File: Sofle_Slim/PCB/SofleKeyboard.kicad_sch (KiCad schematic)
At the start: 103 parts, among them J2 4PIN, J3 OLED, P1 i2c_pin, P2 i2c_pin, P3 USB_C_Plug_USB2.0, SW1 SW_PUSH_LED, SW10 SW_PUSH_LED, SW11 SW_PUSH_LED, SW12 SW_PUSH_LED, SW13 SW_PUSH_LED, SW14 SW_PUSH_LED, SW15 SW_PUSH_LED, SW16 SW_PUSH_LED, SW17 SW_PUSH_LED, SW18 SW_PUSH_LED, SW19 SW_PUSH_LED, SW2 SW_PUSH_LED, SW20 SW_PUSH_LED, SW21 SW_PUSH_LED, SW22 SW_PUSH_LED, SW23 SW_PUSH_LED, SW24 SW_PUSH_LED, SW25 Rotary_Encoder_Switch, SW26 SW_PUSH_LED, SW27 SW_PUSH_LED, SW28 SW_PUSH_LED, SW29 SW_PUSH_LED, SW3 SW_PUSH_LED, SW30 SW_PUSH_LED, SW4 SW_PUSH_LED, SW5 SW_PUSH_LED, SW6 SW_PUSH_LED, SW7 SW_PUSH_LED, SW8 SW_PUSH_LED, SW9 SW_PUSH_LED, U1 ProMicro, U2 ATmega32U4-A, Y1 16MHz

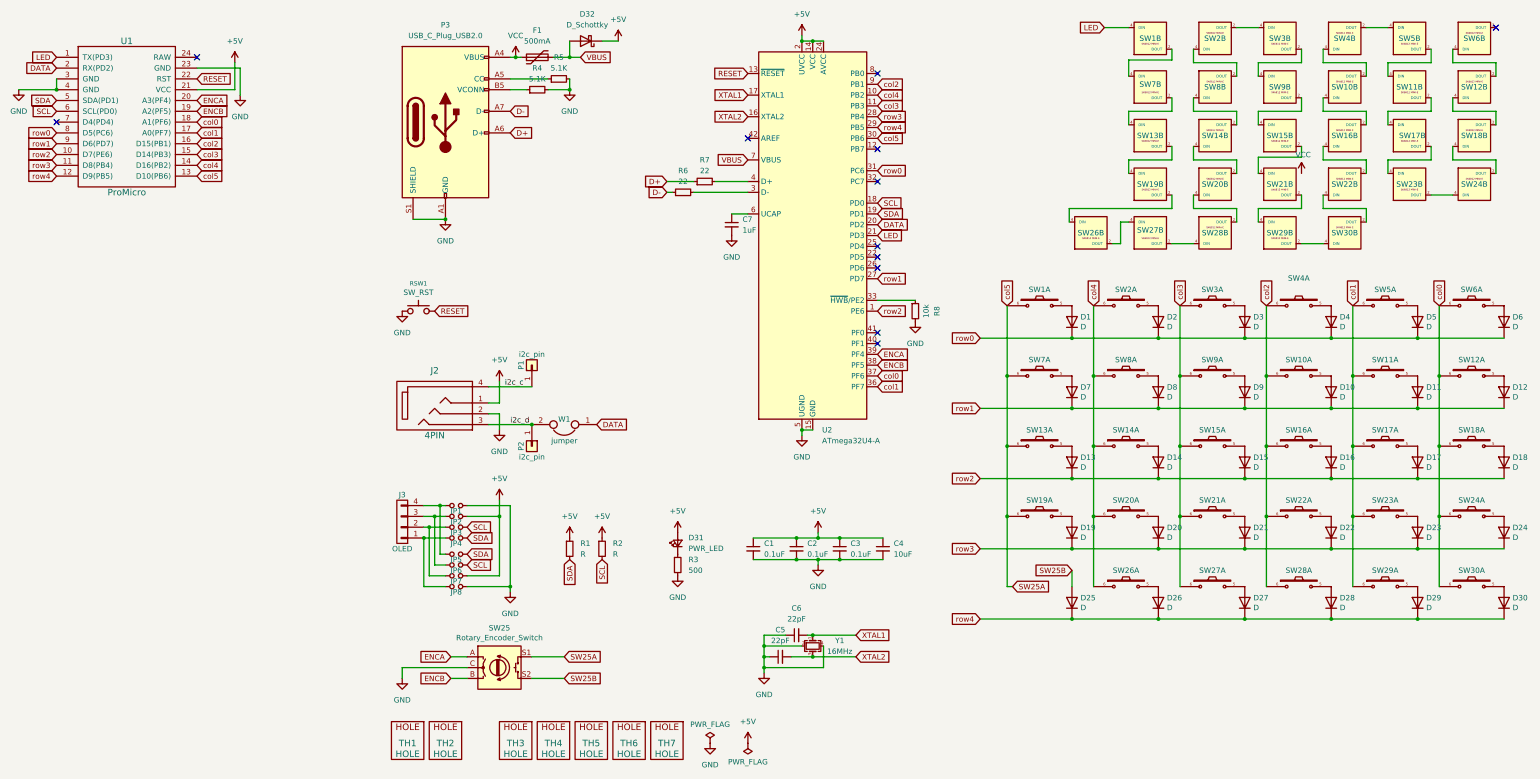
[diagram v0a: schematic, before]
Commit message: changed usb-c plug for usb receptacle
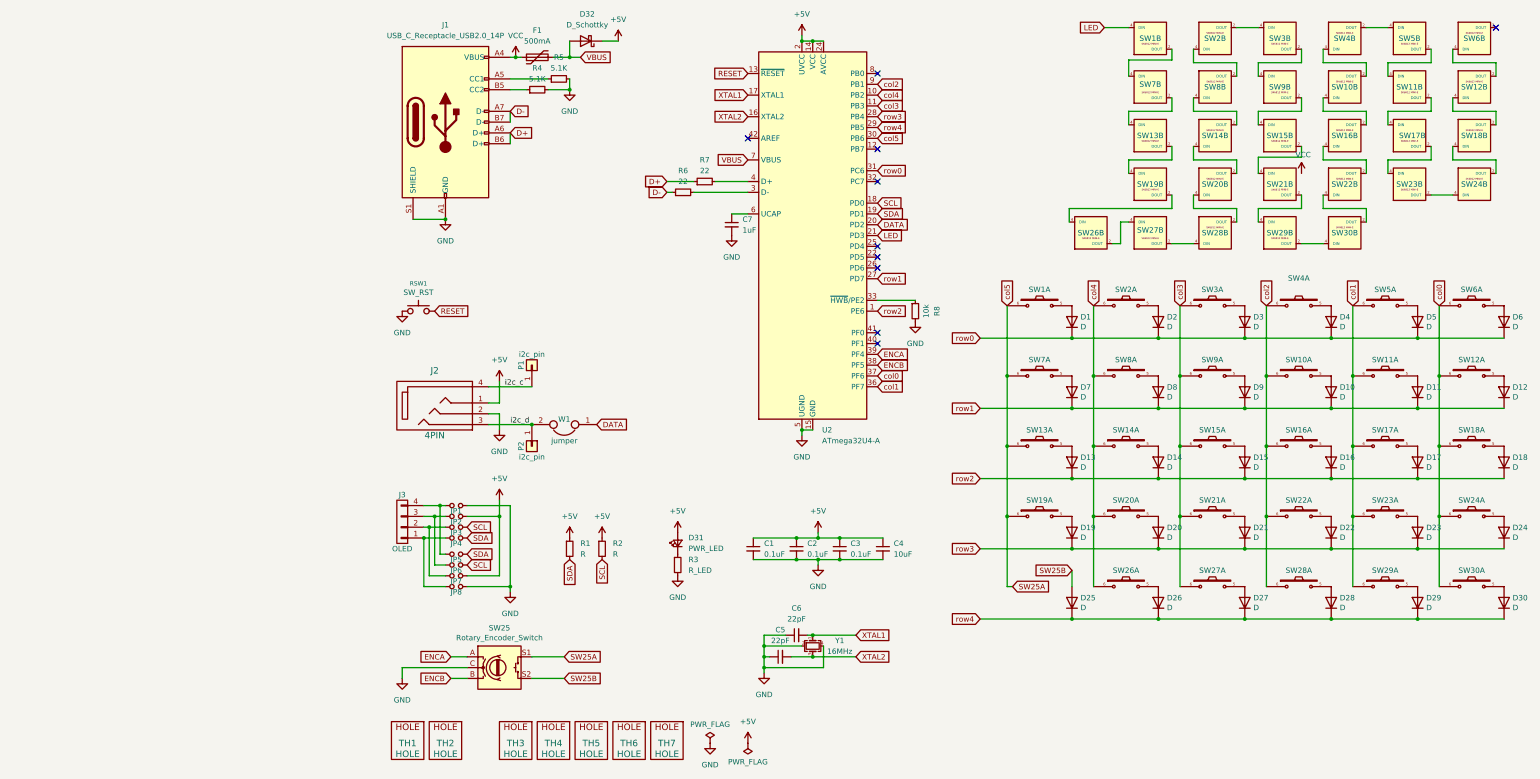
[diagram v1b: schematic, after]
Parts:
- removed P3: USB_C_Plug_USB2.0, symbol Connector:USB_C_Plug_USB2.0
- removed U1: ProMicro, SofleKeyboard-footprint:ProMicro, symbol SofleKeyboard-rescue:ProMicro_2-Lily58-cache-Lily58_Pro-rescue
- added J1: USB_C_Receptacle_USB2.0_14P, Connector_USB:USB_C_Receptacle_GCT_USB4135-GF-A_6P_TopMnt_Horizontal, symbol Connector:USB_C_Receptacle_USB2.0_14P
- C6: footprint (none) -> Capacitor_SMD:C_0805_2012Metric
- D31: footprint (none) -> LED_SMD:LED_0805_2012Metric
- D32: footprint (none) -> Diode_SMD:D_SOD-123F
- R1, R2: footprint (none) -> Resistor_SMD:R_0805_2012Metric
- R3: value 500 -> R_LED; footprint (none) -> Resistor_SMD:R_0805_2012Metric
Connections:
- net D+: now also J1.A6 (D+), J1.B6 (D+)
- net D-: now also J1.A7 (D-), J1.B7 (D-)
- net GND: now also J1.A1 (GND), J1.A12 (GND), J1.B1 (GND), J1.B12 (GND), J1.S1 (SHIELD)
- net VCC: now also J1.A4 (VBUS), J1.A9 (VBUS), J1.B4 (VBUS), J1.B9 (VBUS)
- net at R5.1: now also J1.A5 (CC1)
- net at R4.1: now also J1.B5 (CC2)
- no-connect marks 12 -> 10

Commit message: PCB work in progress
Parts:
- J1: footprint Connector_USB:USB_C_Receptacle_GCT_USB4135-GF-A_6P_TopMnt_Horizontal -> Connector_USB:USB_C_Receptacle_Molex_105450-0101
- R8: value 10k -> 10K
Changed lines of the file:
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@@
       (effects (font (size 1.27 1.27)))
     )
-    (property "Footprint" "Connector_USB:USB_C_Receptacle_GCT_USB4135-GF-A_6P_TopMnt_Horizontal" (at 31.75 44.45 0)
+    (property "Footprint" "Connector_USB:USB_C_Receptacle_Molex_105450-0101" (at 31.75 44.45 0)
       (effects (font (size 1.27 1.27)) hide)
     )
@@
       (effects (font (size 1.27 1.27)))
     )
-    (property "Value" "10k" (at 140.97 88.9 90)
-      (effects (font (size 1.27 1.27)))
-    )
+    (property "Value" "10K" (at 140.97 88.9 90)
+      (effects (font (size 1.27 1.27)))
+    )
